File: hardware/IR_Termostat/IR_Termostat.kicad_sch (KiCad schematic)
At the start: 33 parts, among them J1 USB_C_Receptacle_PowerOnly_6P, J2 JST-PH-2mm, Q1 PMOS, U1 TP4056-42-ESOP8, U2 XC6206P-3.3V, U5 CH32V003JxMx

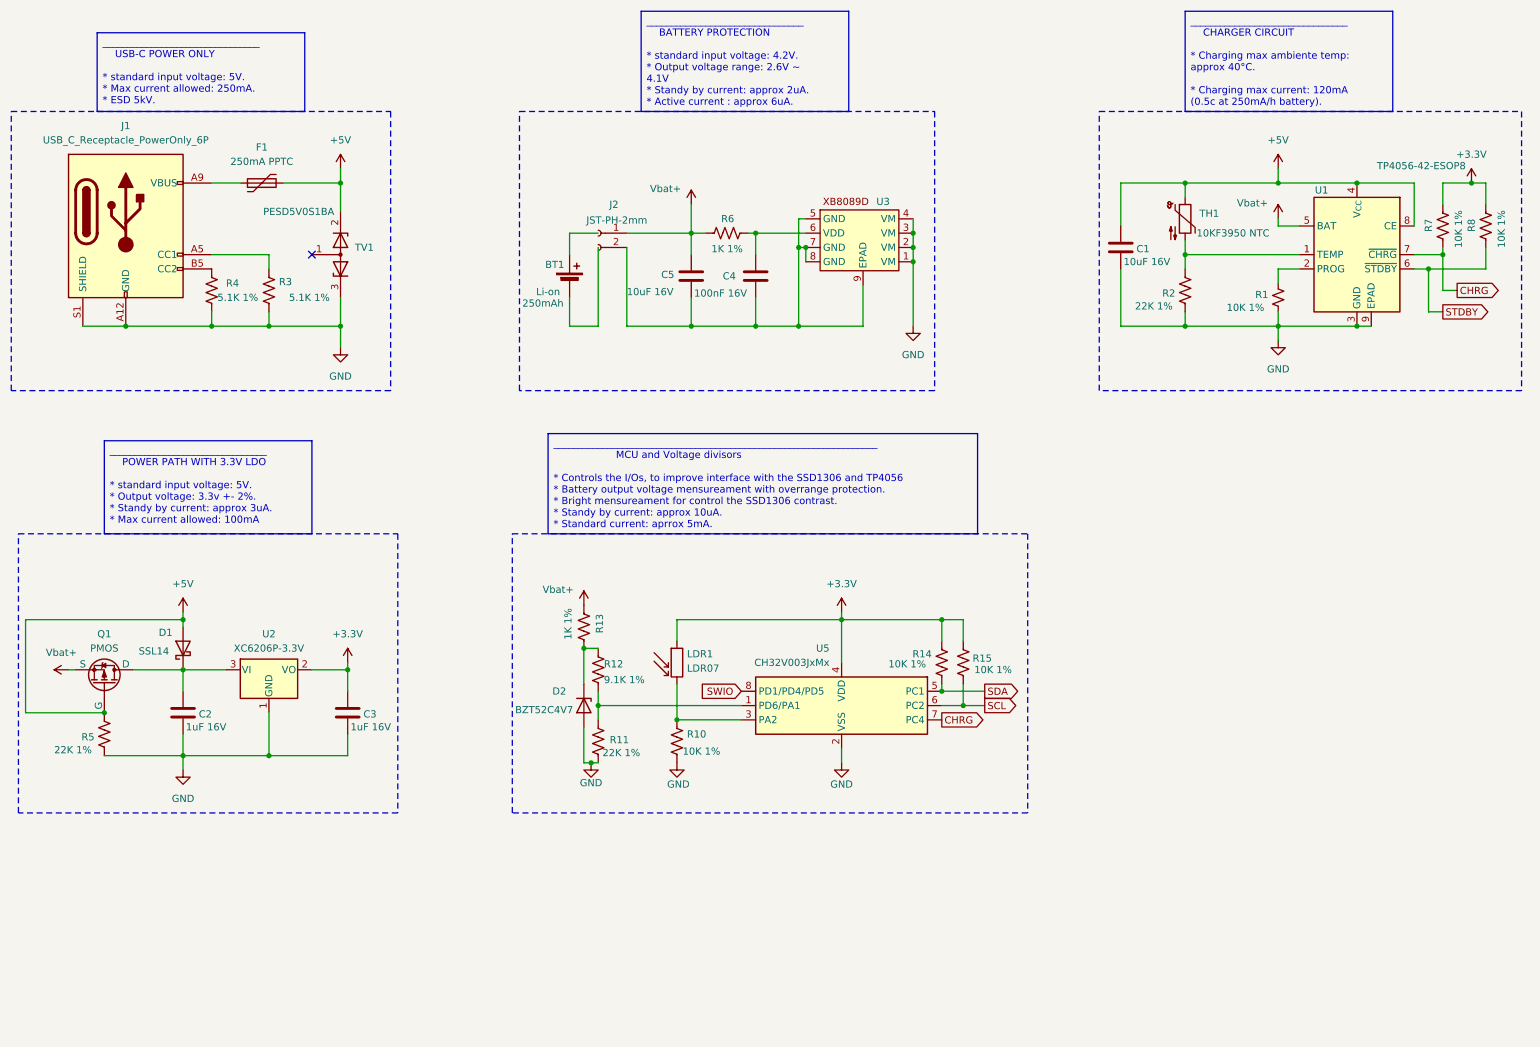
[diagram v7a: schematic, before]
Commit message: Feat: Added I2C Bus peripherals
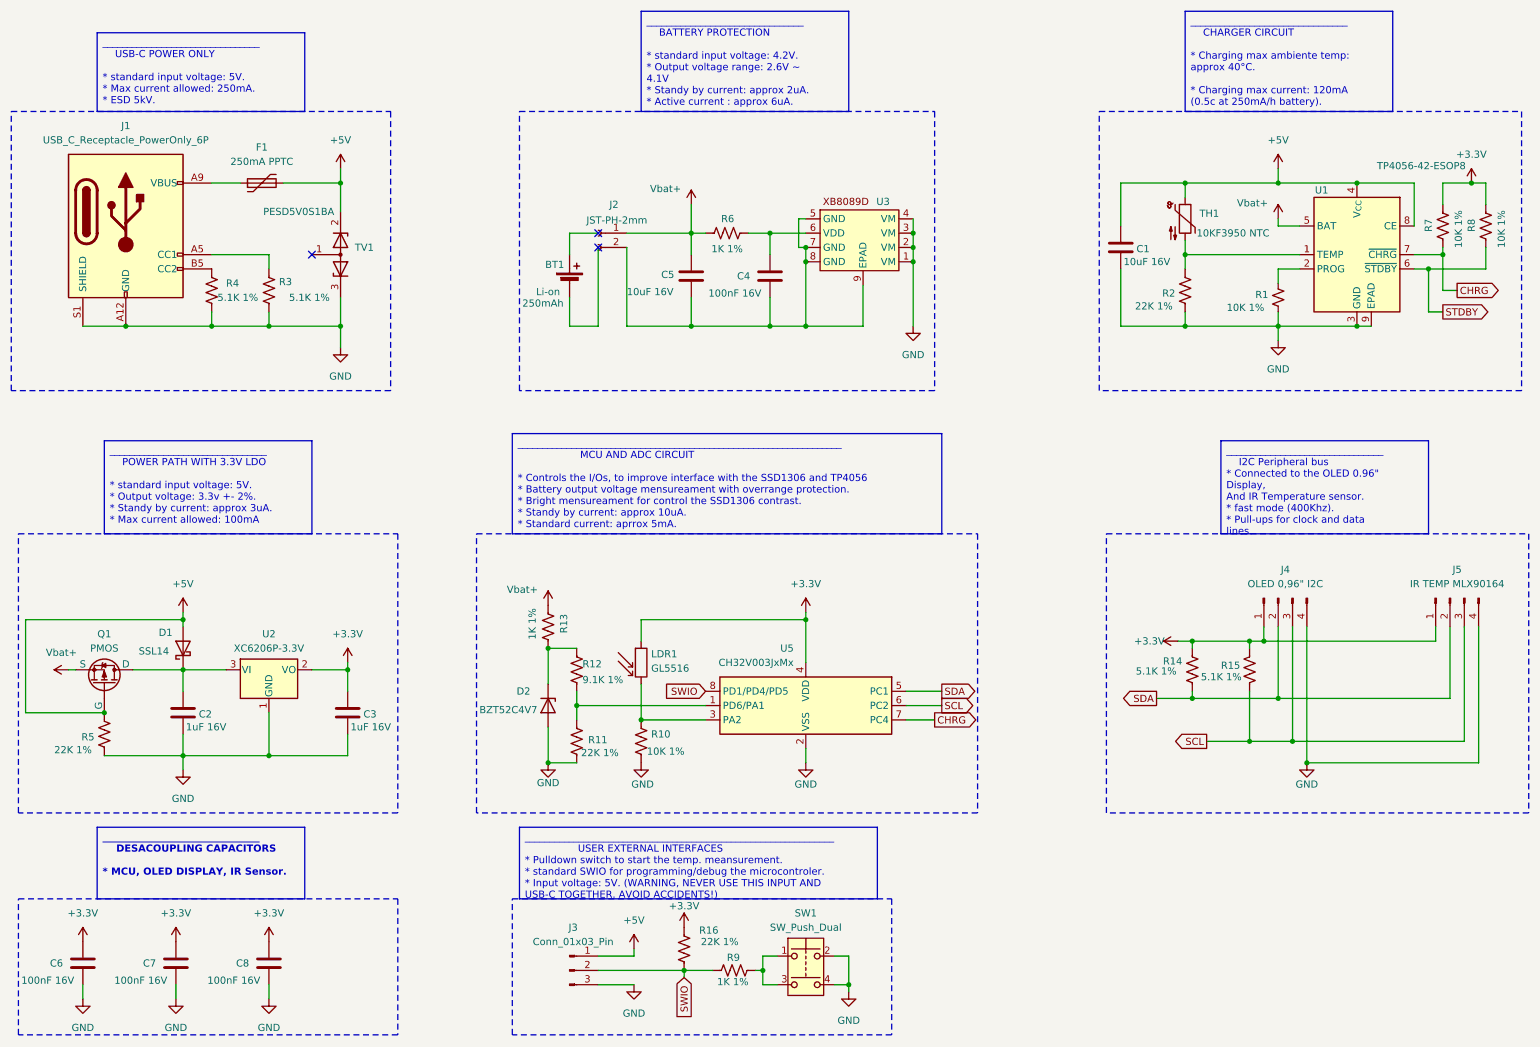
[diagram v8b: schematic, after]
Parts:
- added C6, C7, C8: 100nF 16V, Capacitor_SMD:C_0805_2012Metric_Pad1.18x1.45mm_HandSolder, symbol Device:C
- added J3: Conn_01x03_Pin, symbol Connector:Conn_01x03_Pin
- added J4: OLED 0,96" I2C, Connector_PinSocket_2.54mm:PinSocket_1x04_P2.54mm_Vertical, symbol Connector:Conn_01x04_Pin
- added J5: IR TEMP MLX90164, Connector_PinSocket_2.54mm:PinSocket_1x04_P2.54mm_Vertical, symbol Connector:Conn_01x04_Pin
- added R16: 22K 1%, Resistor_SMD:R_0805_2012Metric_Pad1.20x1.40mm_HandSolder, symbol Device:R_US
- added R9: 1K 1%, Resistor_SMD:R_0805_2012Metric_Pad1.20x1.40mm_HandSolder, symbol Device:R_US
- added SW1: SW_Push_Dual, Button_Switch_SMD:SW_SPST_CK_KMS2xxGP, symbol Switch:SW_Push_Dual
- LDR1: value LDR07 -> GL5516
- R14, R15: value 10K 1% -> 5.1K 1%
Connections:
- net +3.3V: now also C6.1, C7.1, C8.1, J4.1 (Pin_1), J5.1 (Pin_1), R16.2
- net +5V: now also J3.1 (Pin_1)
- net GND: now also C6.2, C7.2, C8.2, J3.3 (Pin_3), J4.4 (Pin_4), J5.4 (Pin_4), SW1.2, SW1.4
- net SCL: now also J4.3 (Pin_3), J5.3 (Pin_3)
- net SDA: now also J4.2 (Pin_2), J5.2 (Pin_2)
- net SWIO: now also J3.2 (Pin_2), R16.1, R9.1
- new net: R9.2, SW1.1, SW1.3
- no-connect marks 1 -> 3
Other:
- moved on the sheet: C4, D2, LDR1, R10, R11, R12, R13, R14, R15, U5
